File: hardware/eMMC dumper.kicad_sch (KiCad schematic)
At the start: 0 parts

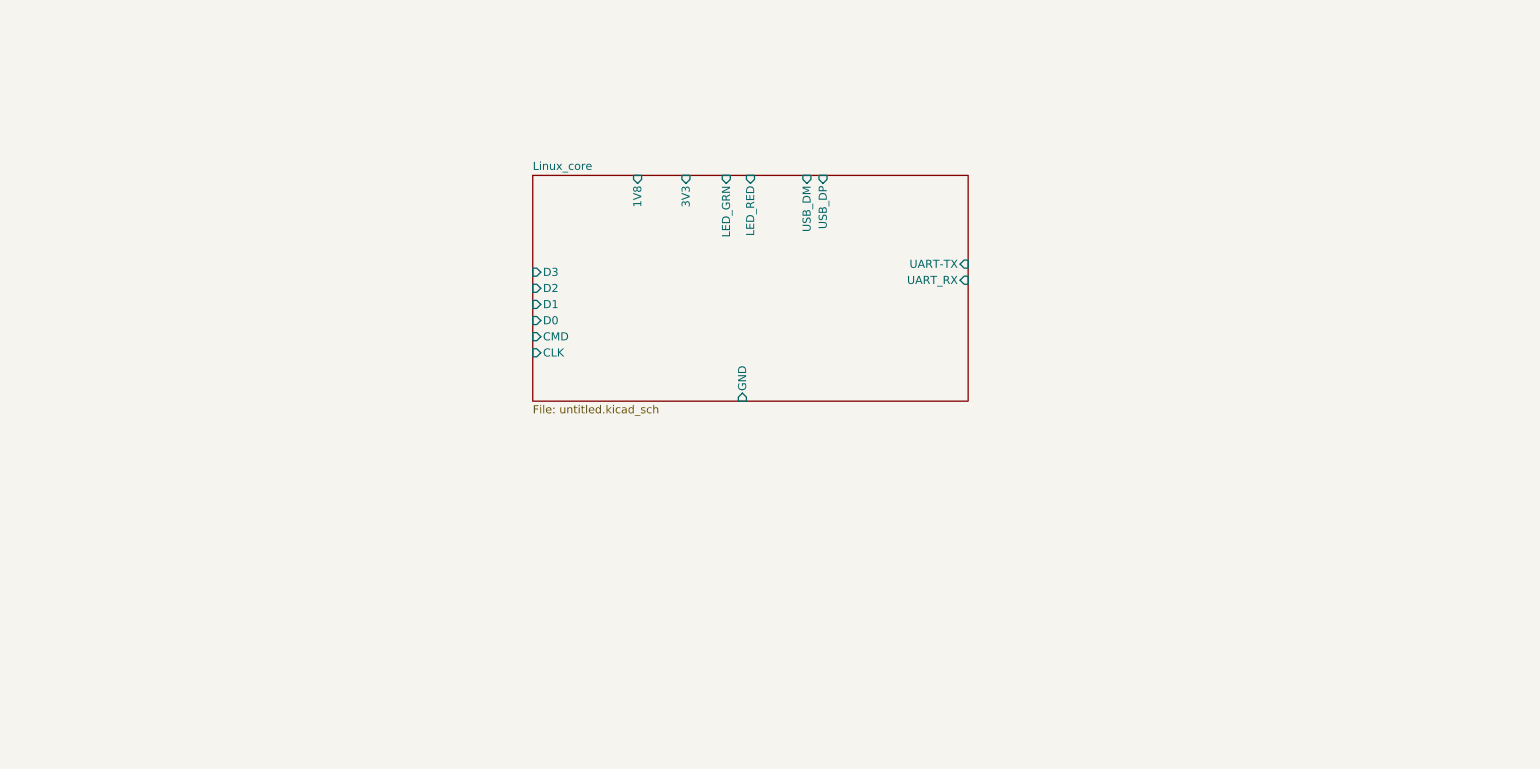
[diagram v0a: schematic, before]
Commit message: Basic schematic
Need to add passives
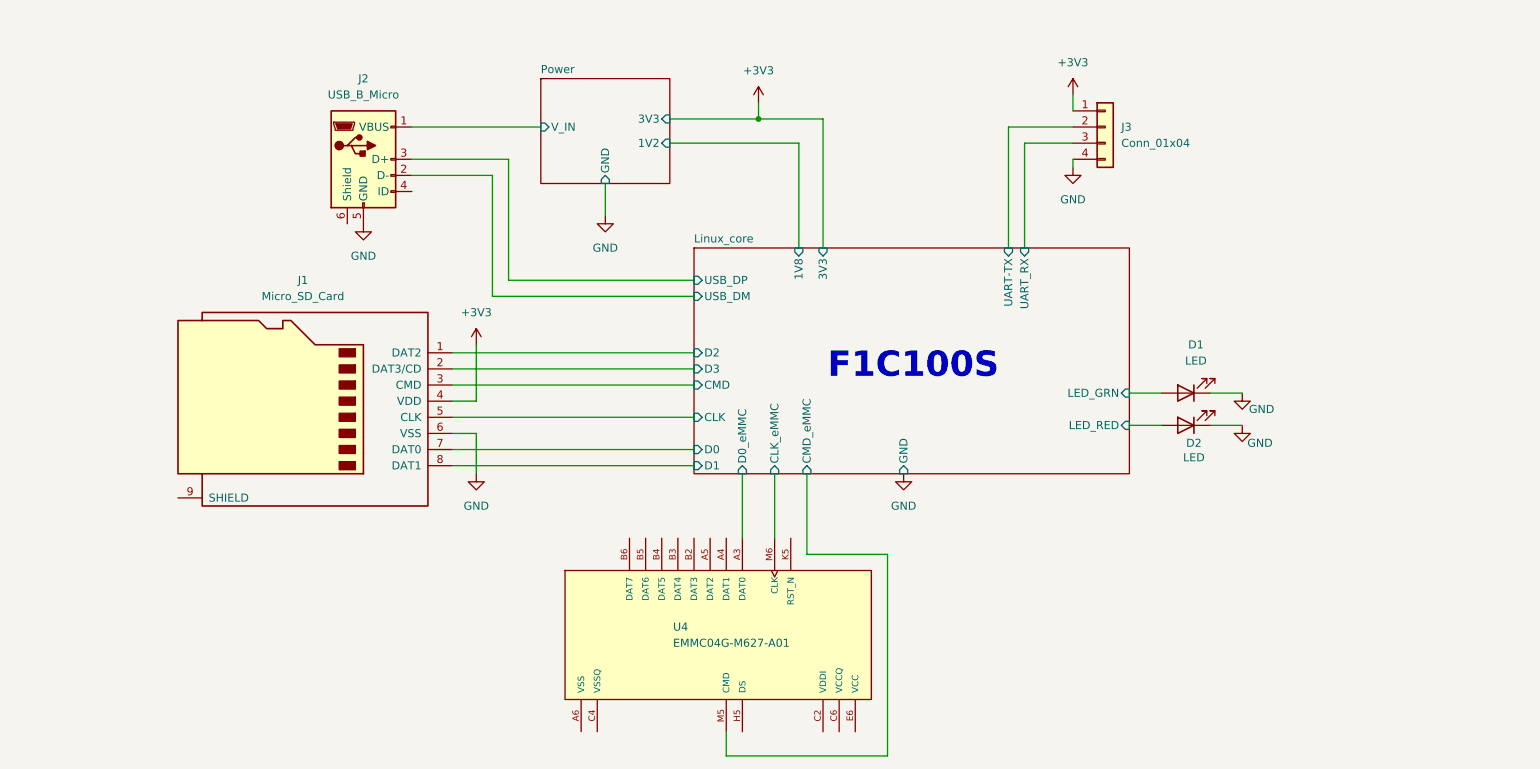
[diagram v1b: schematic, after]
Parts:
- added D1, D2: LED, LED_SMD:LED_0201_0603Metric, symbol Device:LED
- added J1: Micro_SD_Card, symbol Connector:Micro_SD_Card
- added J2: USB_B_Micro, symbol Connector:USB_B_Micro
- added J3: Conn_01x04, symbol Connector_Generic:Conn_01x04
- added U4: EMMC04G-M627-A01, Package_BGA:LFBGA-153_11.5x13mm_Layout14x14_P0.5mm, symbol EMMC04G-M627-A01:EMMC04G-M627-A01
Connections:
- net Linux_core/CLK: now also J1.5 (CLK)
- net Linux_core/CMD: now also J1.3 (CMD)
- net Linux_core/D0: now also J1.7 (DAT0)
- net Linux_core/D1: now also J1.8 (DAT1)
- net Linux_core/D2: now also J1.1 (DAT2)
- net Linux_core/D3: now also J1.2 (DAT3/CD)
- net Linux_core/LED_GRN: now also D1.2 (A)
- net Linux_core/LED_RED: now also D2.2 (A)
- net Linux_core/UART-TX: now also J3.2 (Pin_2)
- net Linux_core/UART_RX: now also J3.3 (Pin_3)
- net Linux_core/USB_DM: now also J2.2 (D-)
- net Linux_core/USB_DP: now also J2.3 (D+)
- new net +3V3: J1.4 (VDD), J3.1 (Pin_1)
- new net GND: D1.1 (K), D2.1 (K), J1.6 (VSS), J2.5 (GND), J3.4 (Pin_4)
- new net Linux_core/CLK_eMMC: U4.M6 (CLK)
- new net Linux_core/CMD_eMMC: U4.M5 (CMD)
- new net Linux_core/D0_eMMC: U4.A3 (DAT0)
- new net Power/V_IN: J2.1 (VBUS)
- new net VCC: U4.E6 (VCC), U4.F5 (VCC), U4.J10 (VCC), U4.K9 (VCC)
- new net VCCQ: U4.C6 (VCCQ), U4.M4 (VCCQ), U4.N4 (VCCQ), U4.P3 (VCCQ), U4.P5 (VCCQ)
- new net VSS: U4.A6 (VSS), U4.E7 (VSS), U4.G5 (VSS), U4.H10 (VSS), U4.J5 (VSS), U4.K8 (VSS)
- new net VSSQ: U4.C4 (VSSQ), U4.N2 (VSSQ), U4.N5 (VSSQ), U4.P4 (VSSQ), U4.P6 (VSSQ)
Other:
- added sheet Power (power.kicad_sch)
- sheet Linux_core ports: added CLK_eMMC, CMD_eMMC, D0_eMMC; removed none
- note added: "F1C100S"

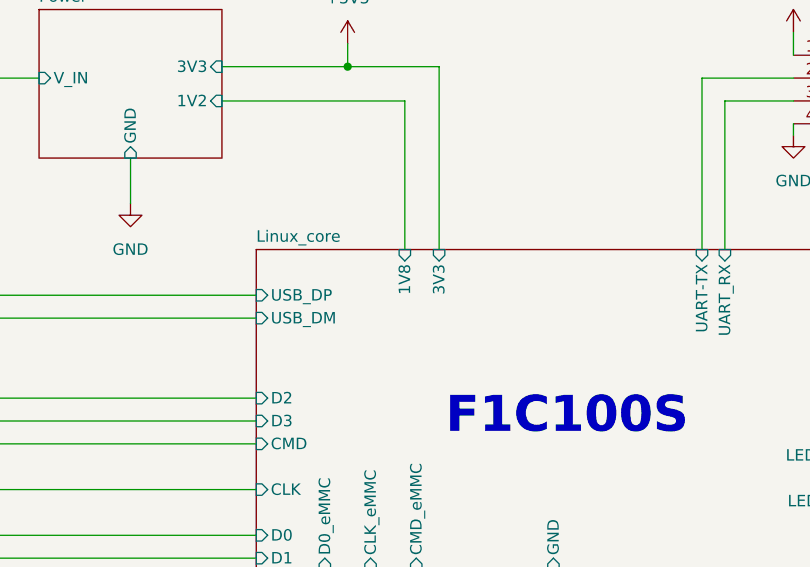
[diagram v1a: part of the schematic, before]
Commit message: added data/clk resistors (33ohm)
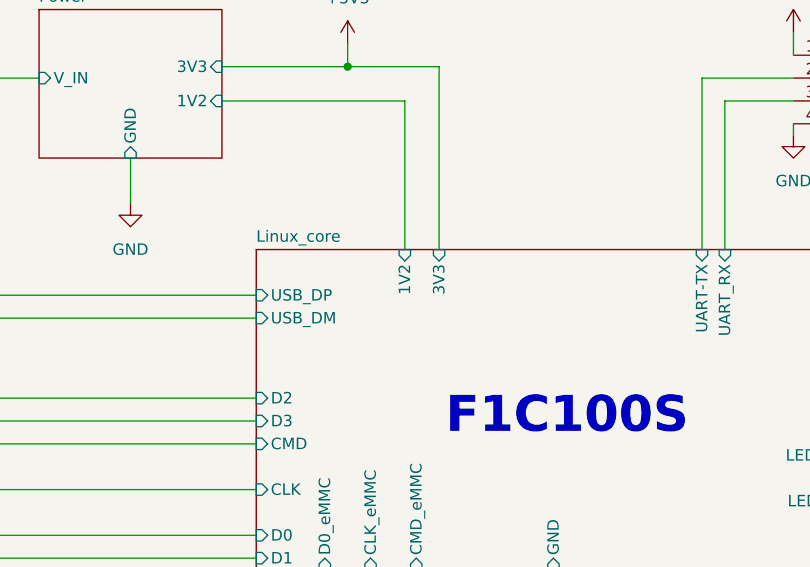
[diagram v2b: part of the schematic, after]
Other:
- sheet Linux_core ports: added 1V2; removed 1V8
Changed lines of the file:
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@@
 			)
 		)
-		(pin "1V8" input
+		(pin "1V2" input
 			(at 152.4 86.36 90)
 			(effects

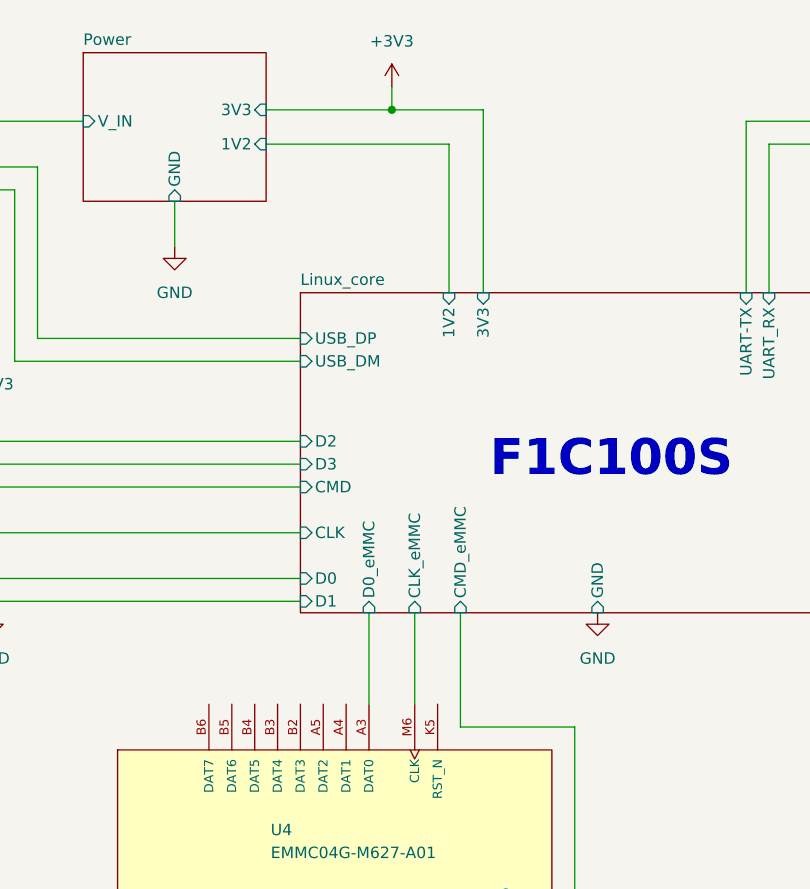
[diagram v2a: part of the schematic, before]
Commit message: Added core decoupling caps
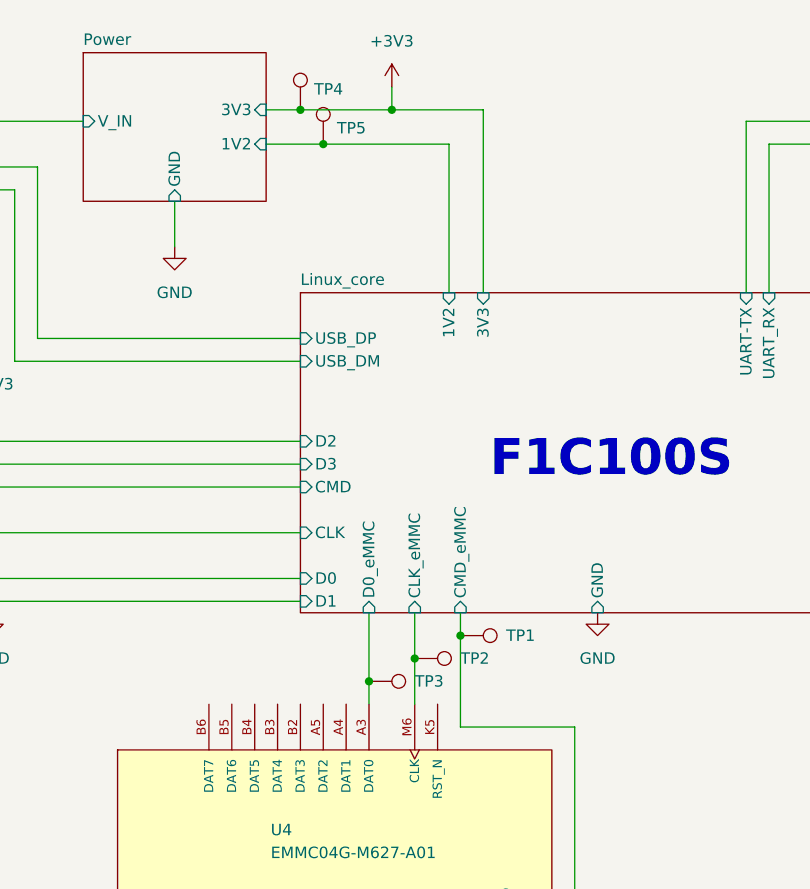
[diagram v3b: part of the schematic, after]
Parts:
- added TP1, TP2, TP3, TP4, TP5: TestPoint, TestPoint:TestPoint_Pad_D1.0mm, symbol Connector:TestPoint
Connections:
- net +3V3: now also TP4.1
- net Linux_core/1V2: now also TP5.1
- net Linux_core/CLK_eMMC: now also TP2.1
- net Linux_core/CMD_eMMC: now also TP1.1
- net Linux_core/D0_eMMC: now also TP3.1

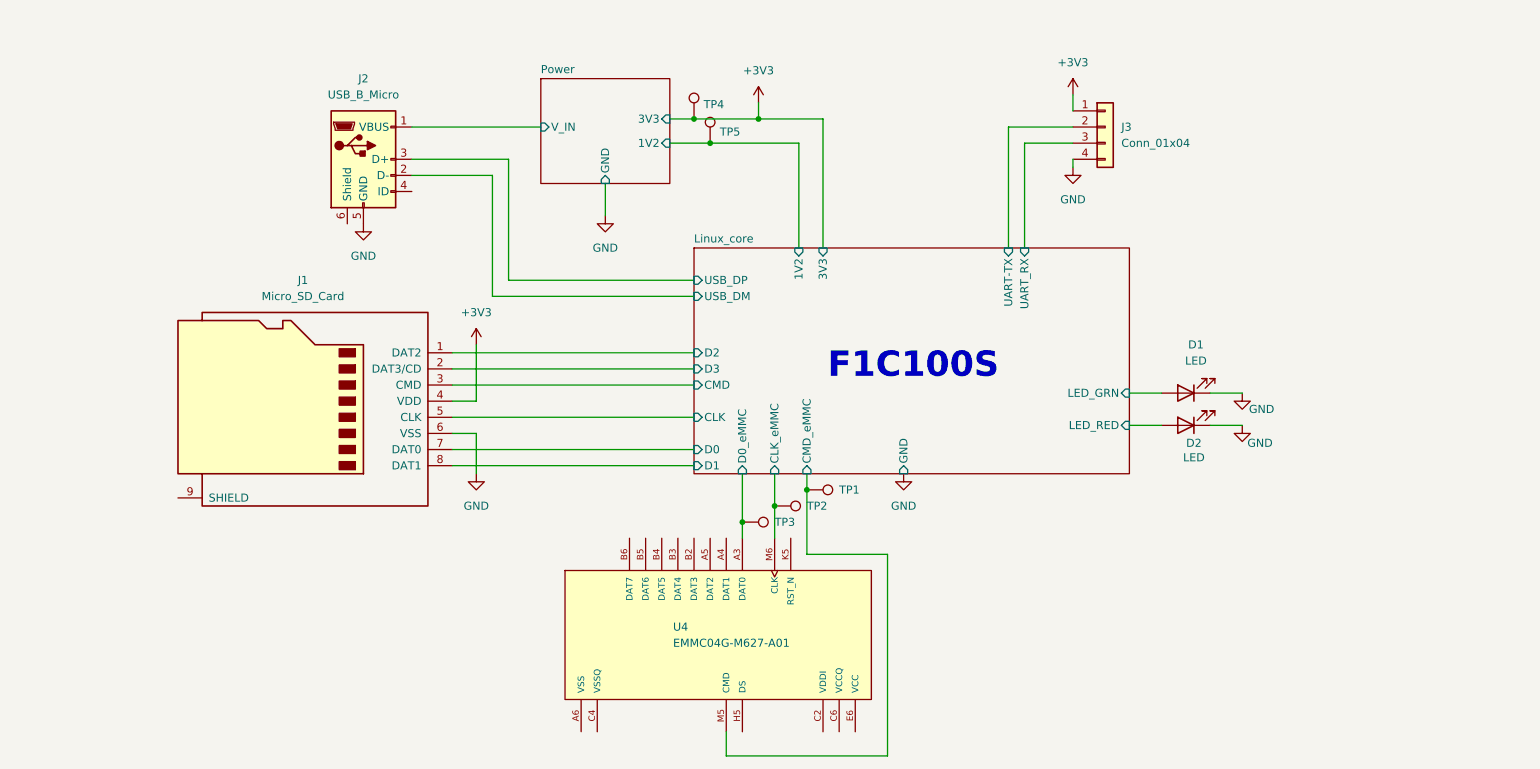
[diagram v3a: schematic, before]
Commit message: Added pullups for SD card
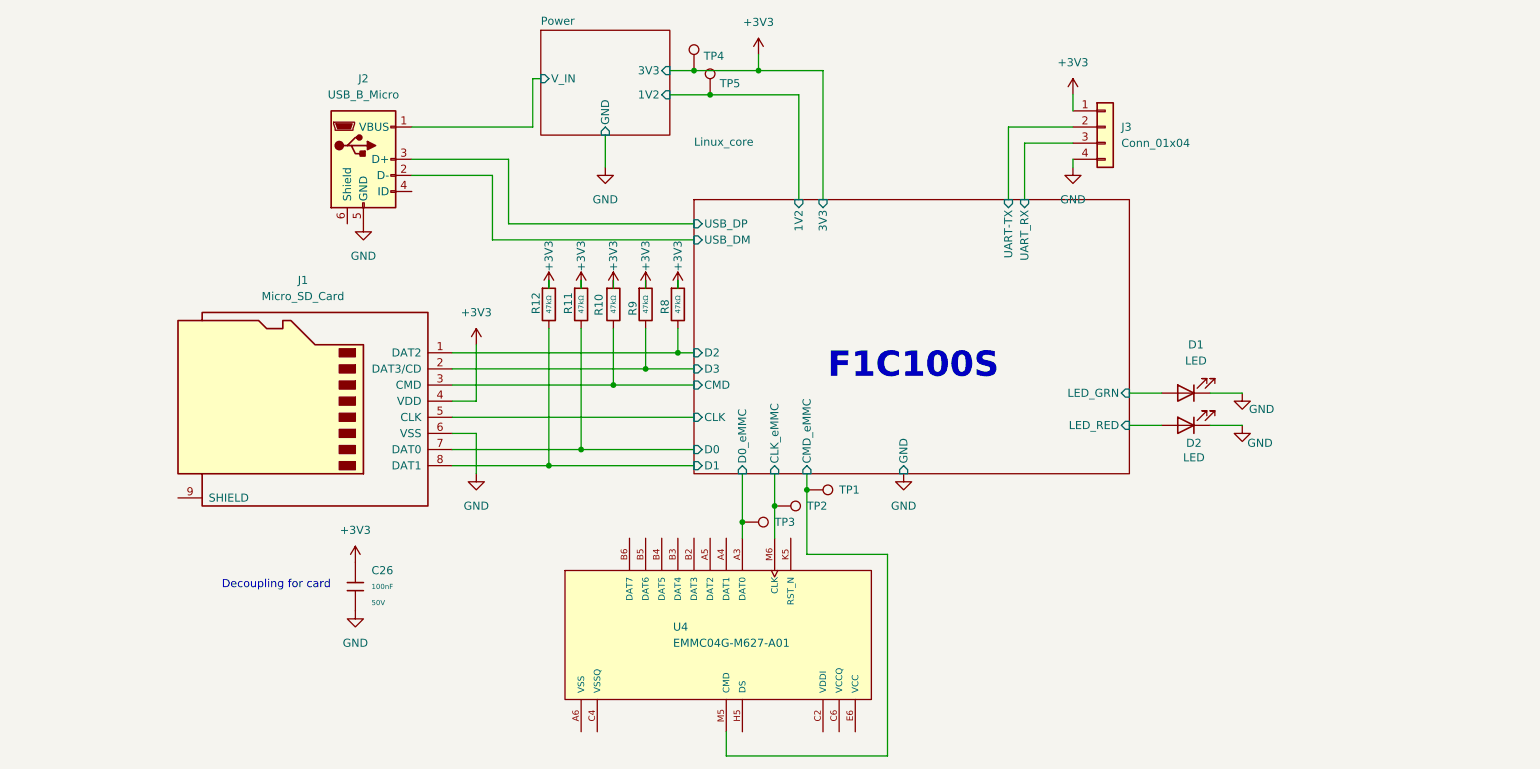
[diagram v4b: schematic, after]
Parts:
- added C26: 100nF, PCM_JLCPCB:C_0603, symbol PCM_JLCPCB-Capacitors:0603,100nF
- added R10, R11, R12, R8, R9: 47kΩ, PCM_JLCPCB:R_0402, symbol PCM_JLCPCB-Resistors:0402,47kΩ
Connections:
- net +3V3: now also C26.1, R10.1, R11.1, R12.1, R8.1, R9.1
- net GND: now also C26.2
- net Linux_core/CMD: now also R10.2
- net Linux_core/D0: now also R11.2
- net Linux_core/D1: now also R12.2
- net Linux_core/D2: now also R8.2
- net Linux_core/D3: now also R9.2
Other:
- note added: "Decoupling for card"
- moved on the sheet: TP4, TP5

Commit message: Board design started
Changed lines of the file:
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@@
 	(text "F1C100S\n"
 		(exclude_from_sim no)
-		(at 170.434 104.902 0)
+		(at 170.18 99.06 0)
 		(effects
 			(font

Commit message: Started placing decoupling capacitors
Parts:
- J1: footprint (none) -> Connector_Card:microSD_HC_Molex_47219-2001
- J2: footprint (none) -> Connector_USB:USB_Micro-AB_Molex_47590-0001
- J3: footprint (none) -> Connector_PinHeader_2.54mm:PinHeader_1x04_P2.54mm_Vertical
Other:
- note added: "LED STATUS -ERROR -READING BOOT0/BOOT1 -READING USER AREA ...perhaps in binary form + silkscreen table"
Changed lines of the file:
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@@
 	(generator_version "9.0")
 	(paper "A4")
+	(text "LED STATUS\n-ERROR\n-READING BOOT0/BOOT1\n-READING USER AREA\n\n...perhaps in binary form\n+ silkscreen table\n"
+		(exclude_from_sim no)
+		(at 251.714 112.522 0)
+		(effects
+			(font
+				(size 1.27 1.27)
+			)
+		)
+	)
 	(text "Decoupling for card"
 		(exclude_from_sim no)
@@
 			)
 		)
-		(property "Footprint" ""
+		(property "Footprint" "Connector_Card:microSD_HC_Molex_47219-2001"
 			(at 45.72 102.87 0)
 			(effects
@@
 			)
 		)
-		(property "Footprint" ""
+		(property "Footprint" "Connector_PinHeader_2.54mm:PinHeader_1x04_P2.54mm_Vertical"
 			(at 200.66 67.31 0)
 			(effects
@@
 			)
 		)
-		(property "Footprint" ""
+		(property "Footprint" "Connector_USB:USB_Micro-AB_Molex_47590-0001"
 			(at 87.63 73.66 0)
 			(effects

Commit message: PCB major changes
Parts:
- removed J3: Conn_01x04, Connector_PinHeader_2.54mm:PinHeader_1x04_P2.54mm_Vertical, symbol Connector_Generic:Conn_01x04
- added D3, D4, D5: LED, LED_SMD:LED_0201_0603Metric, symbol Device:LED
- added H1, H2: MountingHole, MountingHole:MountingHole_3.2mm_M3, symbol Mechanical:MountingHole
- added R17: 1kΩ, PCM_JLCPCB:R_0603, symbol PCM_JLCPCB-Resistors:0603,1kΩ
- added TP6, TP7, TP8: TestPoint, TestPoint:TestPoint_Pad_D1.0mm, symbol Connector:TestPoint
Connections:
- net +3V3: now also R17.2
- net GND: now also D3.1 (K), D4.1 (K), D5.1 (K), TP8.1
- net Linux_core/UART-TX: now also TP6.1
- net Linux_core/UART_RX: now also TP7.1
- net Linux_core/LED_GRN renamed Linux_core/LED_1
- net Linux_core/LED_RED renamed Linux_core/LED_2
- new net: D5.2 (A), R17.1
- new net Linux_core/LED_3: D3.2 (A)
- new net Linux_core/LED_4: D4.2 (A)
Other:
- sheet Linux_core ports: added LED_1, LED_2, LED_3, LED_4; removed LED_GRN, LED_RED
- moved on the sheet: D1, D2, TP4
